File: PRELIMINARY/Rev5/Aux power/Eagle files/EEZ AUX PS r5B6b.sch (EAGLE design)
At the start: 66 parts, among them IC1 LM25575, IC2 UA78M12DCY, IC3 TPD4E002DRLR, IC4 TPD2E001DZDR, Q1 BTA26-600, Q2 BTA26-600, Q3 IRLL014N, X1 282836-5, X2 09185067324, X3 22-23-2031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

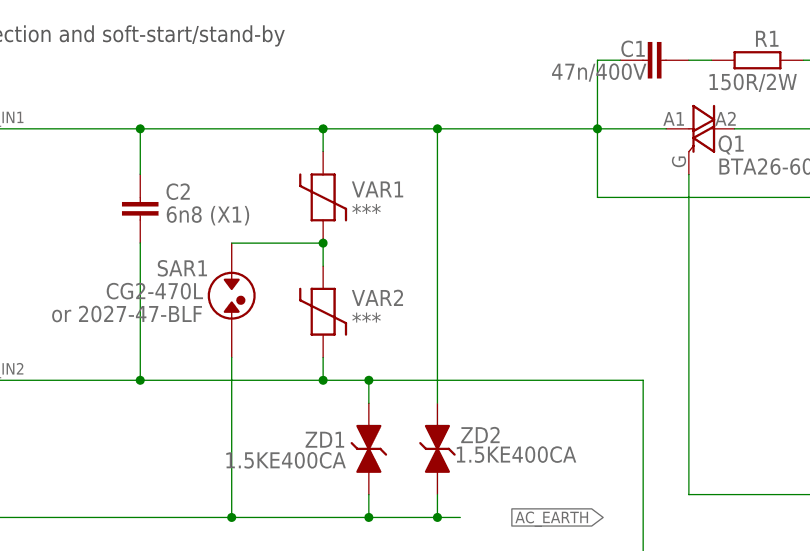
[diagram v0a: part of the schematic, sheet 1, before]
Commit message: AUX PS r5B6b - added extra mounting tab
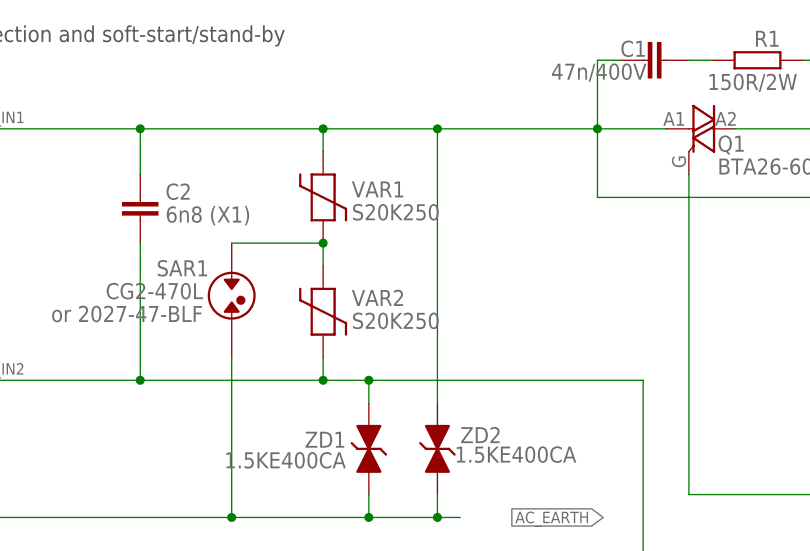
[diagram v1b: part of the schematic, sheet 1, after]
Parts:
- VAR1, VAR2: value *** -> S20K250
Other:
- note added: "Farnell: 1004387, TME: SIOV-S20K140"
- note added: "S20K140"
- note removed: "***"
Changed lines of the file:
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@@
 <part name="P+2" library="supply1" deviceset="+5V" device=""/>
 <part name="TR1" library="EEZ_Lib1" deviceset="PCB_TRAFO6VA_TEZ+VPP" device="" value="TEZ6/D230/15V"/>
-<part name="VAR1" library="EEZ_Lib1" deviceset="VARISTOR" device="" value="***"/>
-<part name="VAR2" library="EEZ_Lib1" deviceset="VARISTOR" device="" value="***"/>
+<part name="VAR1" library="EEZ_Lib1" deviceset="VARISTOR" device="" value="S20K250"/>
+<part name="VAR2" library="EEZ_Lib1" deviceset="VARISTOR" device="" value="S20K250"/>
 <part name="C2" library="rcl" deviceset="C-EU" device="102-064X133" value="6n8 (X1)"/>
 </parts>
@@
 <text x="26.67" y="34.925" size="1.6764" layer="103">2027-23-BLF</text>
 <text x="44.45" y="34.925" size="1.6764" layer="103">Farnell: 1780455, TME: CG2-230L</text>
-<text x="26.67" y="24.765" size="1.6764" layer="103">***</text>
+<text x="26.67" y="24.765" size="1.6764" layer="103">S20K140</text>
 <text x="26.67" y="32.385" size="1.6764" layer="103">VPP28-180</text>
 <text x="44.45" y="27.305" size="1.6764" layer="103">Newark: 37B9209</text>
-<text x="44.45" y="24.765" size="1.6764" layer="103">***</text>
+<text x="44.45" y="24.765" size="1.6764" layer="103">Farnell: 1004387, TME: SIOV-S20K140</text>
 <wire x1="7.62" y1="40.64" x2="25.4" y2="40.64" width="0.1524" layer="103"/>
 <wire x1="25.4" y1="40.64" x2="43.18" y2="40.64" width="0.1524" layer="103"/>
